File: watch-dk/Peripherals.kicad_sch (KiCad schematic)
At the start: 46 parts, among them IC501 APDS-9306-065, IC502 BMI270, IC503 LIS2MDLTR, IC504 BMP581, IC505 DRV2603RUNT, IC506 RV-8263-C8, IC507 PCA9306JK, J501 Jumper, J502 Jumper, J503 Jumper, J504 Jumper, J505 Jumper, J506 Jumper, J507 Jumper, M501 Vibrator DC Motor, Q501 PMZB320UPEYL, X501 Current, X502 I2S, X503 Current, X504 I2C, X505 Current, X506 Current, X507 Current, X508 Current, X509 Motor, X510 Current

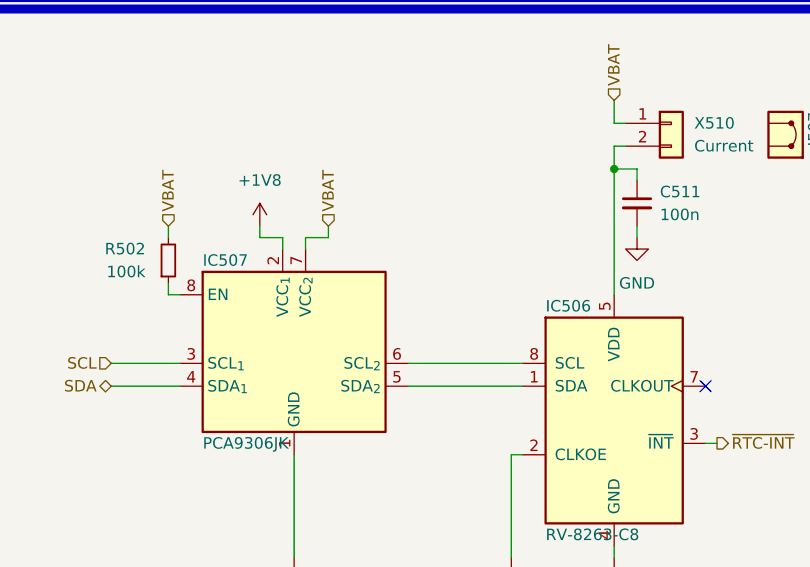
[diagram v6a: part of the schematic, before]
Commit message: Bug: Issue #134
Signed-off-by: Daniel Kampert <DanielKampert@kampis-elektroecke.de>
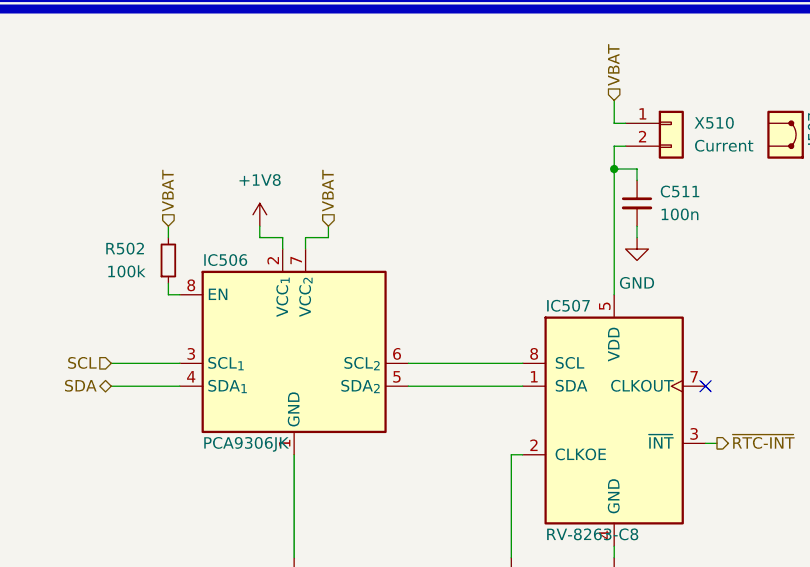
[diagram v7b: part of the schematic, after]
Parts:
- renumbered IC507 to IC506, IC506 to IC507
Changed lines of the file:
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@@
 		(on_board yes)
 		(dnp no)
-		(property "Reference" "IC506"
+		(property "Reference" "IC507"
 			(at 373.38 125.73 0)
 			(effects
@@
 			(project "Dev-Kit"
 				(path "/d5742f03-3b1a-42e5-a384-018bd4b919aa/c5103ceb-5325-4a84-a025-9638a412984e/82af773f-8c39-43b9-baa2-3658da6c8bb2"
-					(reference "IC506")
+					(reference "IC507")
 					(unit 1)
 				)
@@
 		(dnp no)
 		(fields_autoplaced yes)
-		(property "Reference" "#PWR0538"
+		(property "Reference" "#PWR0537"
 			(at 341.63 120.65 0)
 			(effects
@@
 			(project "Watch-DK"
 				(path "/d5742f03-3b1a-42e5-a384-018bd4b919aa/c5103ceb-5325-4a84-a025-9638a412984e/82af773f-8c39-43b9-baa2-3658da6c8bb2"
-					(reference "#PWR0538")
+					(reference "#PWR0537")
 					(unit 1)
 				)
@@
 		(on_board yes)
 		(dnp no)
-		(property "Reference" "#PWR0537"
+		(property "Reference" "#PWR0538"
 			(at 345.44 160.02 0)
 			(effects
@@
 			(project "Watch-DK"
 				(path "/d5742f03-3b1a-42e5-a384-018bd4b919aa/c5103ceb-5325-4a84-a025-9638a412984e/82af773f-8c39-43b9-baa2-3658da6c8bb2"
-					(reference "#PWR0537")
+					(reference "#PWR0538")
 					(unit 1)
 				)
@@
 		(on_board yes)
 		(dnp no)
-		(property "Reference" "IC507"
+		(property "Reference" "IC506"
 			(at 335.28 120.65 0)
 			(effects
@@
 			(project ""
 				(path "/d5742f03-3b1a-42e5-a384-018bd4b919aa/c5103ceb-5325-4a84-a025-9638a412984e/82af773f-8c39-43b9-baa2-3658da6c8bb2"
-					(reference "IC507")
+					(reference "IC506")
 					(unit 1)
 				)

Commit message: doc: CI/CD fixes, documentation updates
- Fix wrong part number for SWD connector
- Fix missing footprint for RTC level shifter

Signed-off-by: Daniel Kampert <DanielKampert@kampis-elektroecke.de>
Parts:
- IC506: footprint https://www.nxp.com/docs/en/data-sheet/PCA9306.pdf -> Package_SON_Kampi:XSON-8_0.65x0.17mm_P0.35mm; manf# PCA9306JK -> PCA9306JKZ
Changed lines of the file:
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@@
 			)
 		)
-		(property "Footprint" "https://www.nxp.com/docs/en/data-sheet/PCA9306.pdf"
+		(property "Footprint" "Package_SON_Kampi:XSON-8_0.65x0.17mm_P0.35mm"
 			(at 345.44 130.81 0)
 			(effects
@@
 			)
 		)
-		(property "manf#" "PCA9306JK"
+		(property "manf#" "PCA9306JKZ"
 			(at 345.44 130.81 0)
 			(effects
